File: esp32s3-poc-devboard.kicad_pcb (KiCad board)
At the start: 4 copper layers, 98 parts, among them J1 24VDC, J2 Conn_01x01_Pin, J3 USB_C_Receptacle_USB2.0_14P, J4 USB_C_Receptacle_USB2.0_14P, J5 Screw_Terminal_01x06, J6 Conn_Coaxial, J7 Conn_01x16_Pin, J8 Screw_Terminal_01x04, Q3 MMDT5551, SW1 SW_Push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

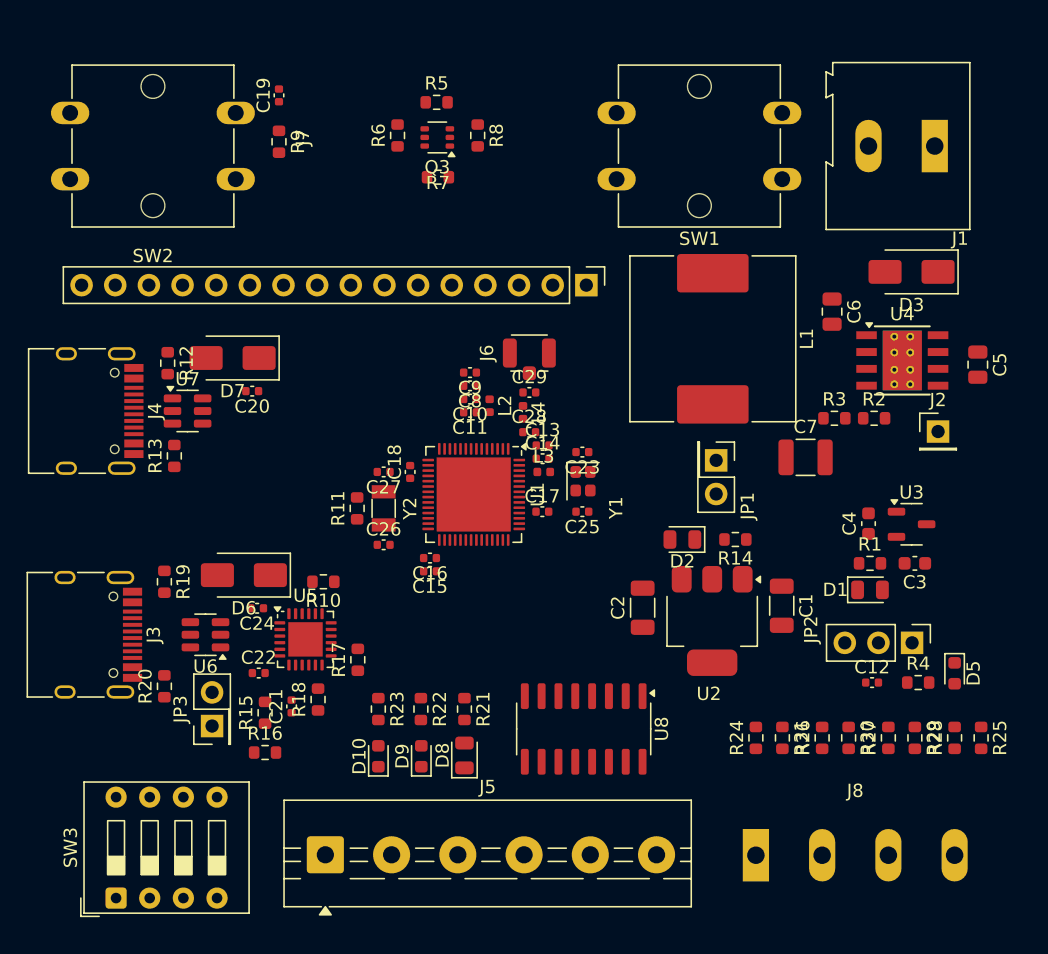
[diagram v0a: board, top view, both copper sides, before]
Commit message: clean up silkscreen
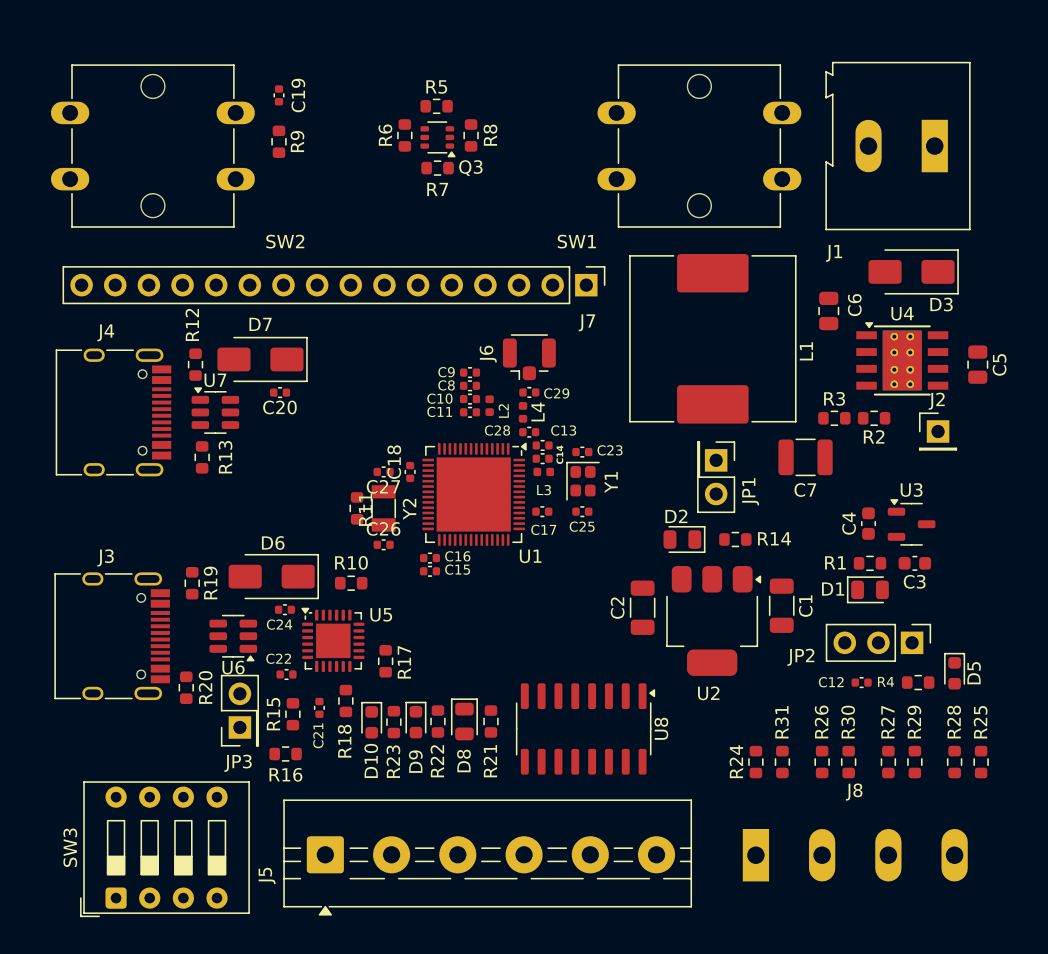
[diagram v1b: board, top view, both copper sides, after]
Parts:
- moved D10 2.61 mm to (147.5, 102.0), turned to -90 degrees
- moved D9 2.60 mm to (150.8, 102.0), turned to -90 degrees
- moved D8 2.56 mm to (154.5, 101.9), turned to -90 degrees
- moved R21 2.21 mm to (156.5, 101.9)
- moved C20 2.10 mm to (140.6, 77.1)
- moved C21 2.10 mm to (143.6, 100.9)
- moved JP3 2.10 mm to (137.6, 102.4)
- moved R15 2.10 mm to (141.6, 101.4)
- moved R17 2.10 mm to (148.6, 97.4)
- moved R18 2.10 mm to (145.6, 100.4)
- moved U6 2.10 mm to (137.1, 95.5)
- moved C22 2.10 mm to (141.1, 98.4)
- moved C24 2.10 mm to (140.9, 93.5)
- moved D6 2.10 mm to (139.9, 91.0)
- moved D7 2.10 mm to (139.1, 74.6)
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
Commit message: add board outline
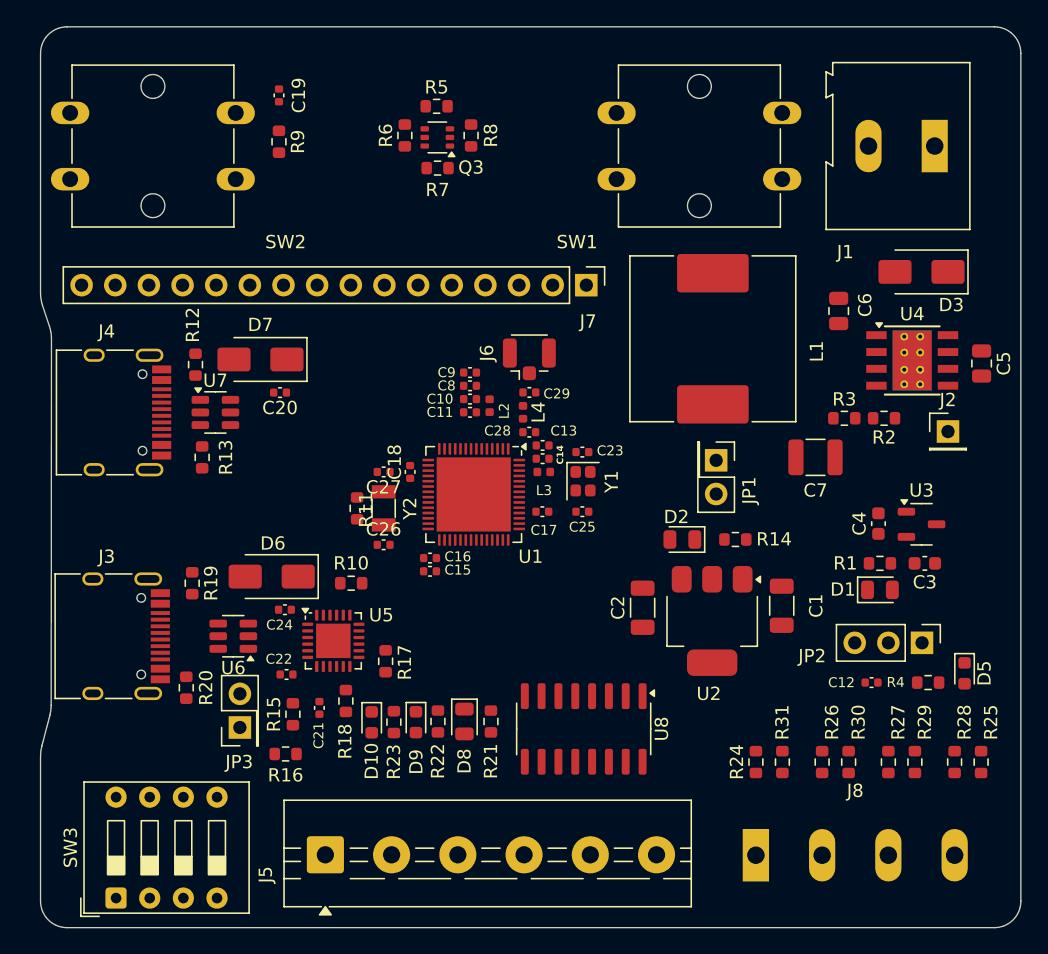
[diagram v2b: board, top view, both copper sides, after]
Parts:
- moved C12 0.75 mm to (185.2, 99.0)
- moved C3 0.75 mm to (189.2, 90.0)
- moved C4 0.75 mm to (185.8, 87.0)
- moved C6 0.75 mm to (182.8, 71.0)
- moved C7 0.75 mm to (181.0, 82.0)
- moved D1 0.75 mm to (185.9, 92.0)
- moved D3 0.75 mm to (189.0, 68.0)
- moved D5 0.75 mm to (192.2, 98.3)
- moved J2 0.75 mm to (191.0, 80.0)
- moved JP2 0.75 mm to (189.0, 96.0)
- moved R1 0.75 mm to (185.9, 90.0)
- moved R2 0.75 mm to (186.2, 79.0)
- moved R3 0.75 mm to (183.2, 79.0)
- moved R4 0.75 mm to (189.5, 99.0)
- moved U3 0.75 mm to (189.0, 87.0)
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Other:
- board outline added: 74 x 68 mm

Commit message: add inner ground layers
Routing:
- added copper zone on In1.Cu, net GND
- added copper zone on In2.Cu, net GND
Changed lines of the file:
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@@
 		(6 "In2.Cu" signal)
 		(2 "B.Cu" signal)
-		(9 "F.Adhes" user "F.Adhesive")
 		(11 "B.Adhes" user "B.Adhesive")
 		(13 "F.Paste" user)
@@
 		(1 "F.Mask" user)
 		(3 "B.Mask" user)
-		(17 "Dwgs.User" user "User.Drawings")
-		(19 "Cmts.User" user "User.Comments")
-		(21 "Eco1.User" user "User.Eco1")
-		(23 "Eco2.User" user "User.Eco2")
 		(25 "Edge.Cuts" user)
 		(27 "Margin" user)
@@
 		(layer "Edge.Cuts")
 	)
+	(zone
+		(net 1)
+		(net_name "GND")
+		(layers "In1.Cu" "In2.Cu")
+		(hatch edge 0.5)
+		(connect_pads
+			(clearance 0.3)
+		)
+		(min_thickness 0.15)
+		(filled_areas_thickness no)
+		(fill yes
+			(thermal_gap 0.4)
+			(thermal_bridge_width 0.25)
+		)
+		(polygon
+			(pts
+				(xy 196.5 49.5) (xy 196.5 117.5) (xy 122.5 117.5) (xy 122.5 49.5)
+			)
+		)
+	)
 	(embedded_fonts no)

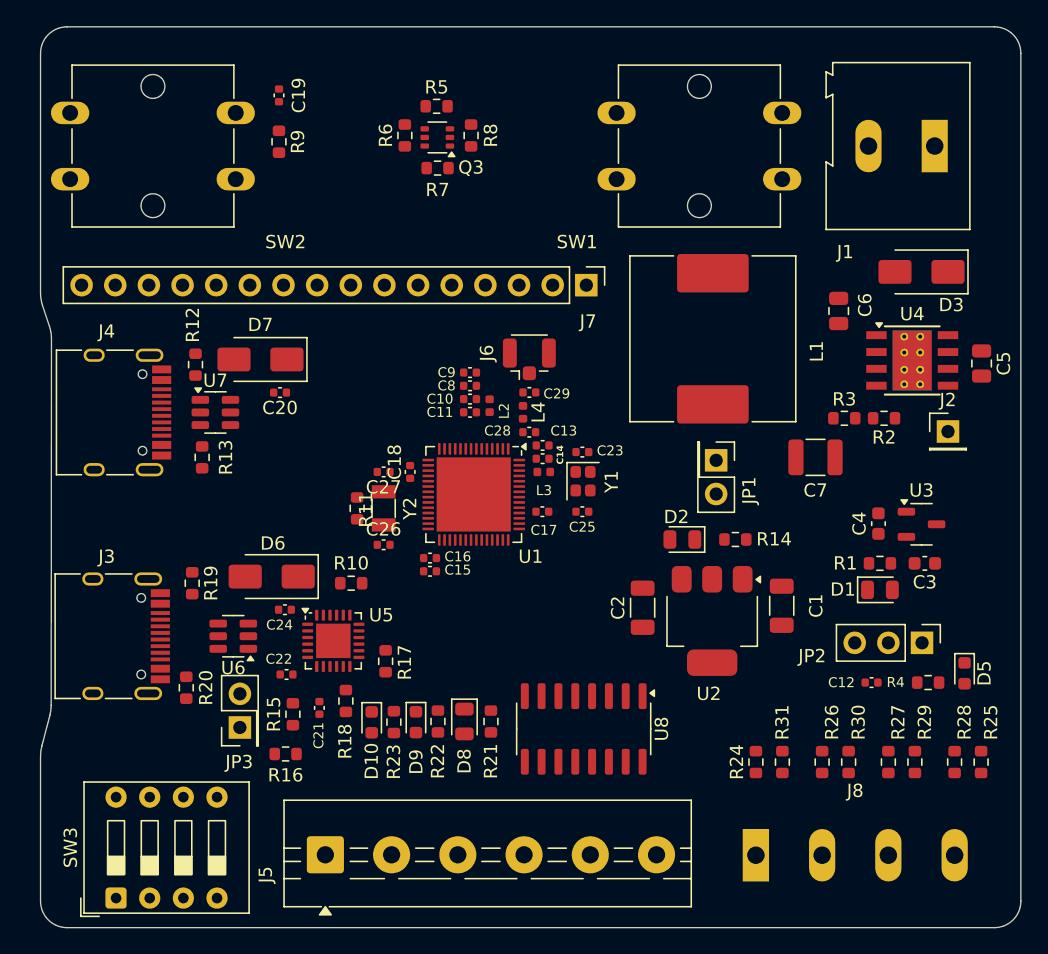
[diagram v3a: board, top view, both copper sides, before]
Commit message: add jlc tooling holes
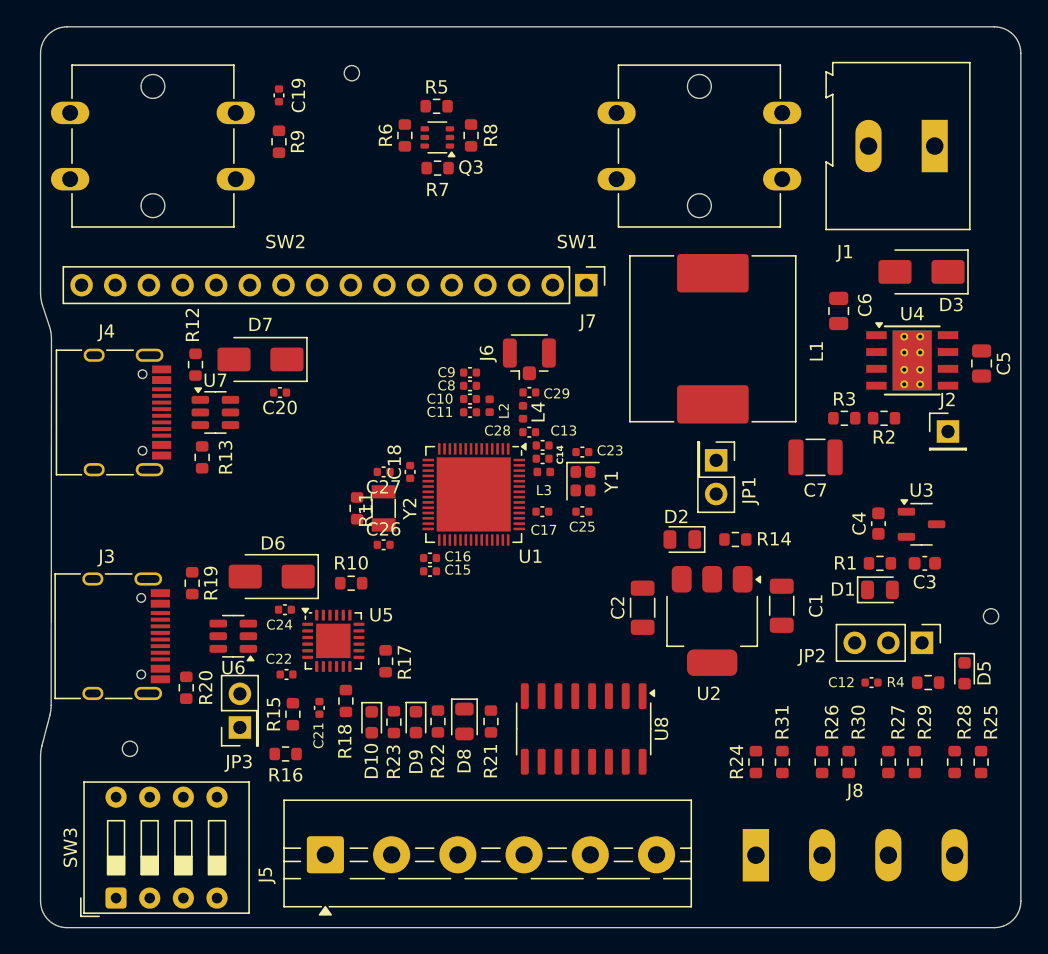
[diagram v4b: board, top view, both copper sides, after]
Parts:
- added ?: , , F.Cu at (194.2, 94.0)
- added ?: , , F.Cu at (146.0, 53.0)
- added REF**: ToolingHole_1.152mm, MountingHole:ToolingHole_1.152mm, F.Cu at (129.2, 104.0)
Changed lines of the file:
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@@
 		)
 	)
+	(footprint ""
+		(layer "F.Cu")
+		(at 194.25 94)
+		(property "Reference" ""
+			(at 0 0 0)
+			(layer "F.SilkS")
+			(effects
+				(font
+					(size 1.27 1.27)
+					(thickness 0.15)
+				)
+			)
+		)
+		(property "Value" ""
+			(at 0 0 0)
+			(layer "F.Fab")
+			(effects
+				(font
+					(size 1.27 1.27)
+					(thickness 0.15)
+				)
+			)
+		)
+		(property "Datasheet" ""
+			(at 0 0 0)
+			(layer "F.Fab")
+			(hide yes)
+			(effects
+				(font
+					(size 1.27 1.27)
+					(thickness 0.15)
+				)
+			)
+		)
+		(property "Description" ""
+			(at 0 0 0)
+			(layer "F.Fab")
+			(hide yes)
+			(effects
+				(font
+					(size 1.27 1.27)
+					(thickness 0.15)
+				)
+			)
+		)
+		(pad "" np_thru_hole circle
+			(at 0 0)
+			(size 1.152 1.152)
+			(drill 1.152)
+			(layers "F&B.Cu" "*.Mask")
+			(solder_mask_margin 0.074)
+		)
+		(embedded_fonts no)
+	)
 	(footprint "Resistor_SMD:R_0603_1608Metric"
 		(layer "F.Cu")
@@
 		)
 	)
+	(footprint ""
+		(layer "F.Cu")
+		(at 146 53)
+		(property "Reference" ""
+			(at 0 0 0)
+			(layer "F.SilkS")
+			(effects
+				(font
+					(size 1.27 1.27)
+					(thickness 0.15)
+				)
+			)
+		)
+		(property "Value" ""
+			(at 0 0 0)
+			(layer "F.Fab")
+			(effects
+				(font
+					(size 1.27 1.27)
+					(thickness 0.15)
+				)
+			)
+		)
+		(property "Datasheet" ""
+			(at 0 0 0)
+			(layer "F.Fab")
+			(hide yes)
+			(effects
+				(font
+					(size 1.27 1.27)
+					(thickness 0.15)
+				)
+			)
+		)
+		(property "Description" ""
+			(at 0 0 0)
+			(layer "F.Fab")
+			(hide yes)
+			(effects
+				(font
+					(size 1.27 1.27)
+					(thickness 0.15)
+				)
+			)
+		)
+		(pad "" np_thru_hole circle
+			(at 0 0)
+			(size 1.152 1.152)
+			(drill 1.152)
+			(layers "F&B.Cu" "*.Mask")
+			(solder_mask_margin 0.074)
+		)
+		(embedded_fonts no)
+	)
 	(footprint "Resistor_SMD:R_0603_1608Metric"
 		(layer "F.Cu")
@@
 		)
 	)
+	(footprint "MountingHole:ToolingHole_1.152mm"
+		(layer "F.Cu")
+		(at 129.25 104)
+		(descr "Tooling Hole 1.152mm, 1.3mm solder mask, JLCPCB specification, https://jlcpcb.com/help/article/How-to-add-tooling-holes-for-PCB-assembly-order")
+		(tags "mounting")
+		(property "Reference" "REF**"
+			(at 0 -1.5 0)
+			(layer "F.SilkS")
+			(hide yes)
+			(effects
+				(font
+					(size 1 1)
+					(thickness 0.15)
+				)
+			)
+		)
+		(property "Value" "ToolingHole_1.152mm"
+			(at 0 1.6 0)
+			(layer "F.Fab")
+			(effects
+				(font
+					(size 1 1)
+					(thickness 0.15)
+				)
+			)
+		)
+		(property "Datasheet" ""
+			(at 0 0 0)
+			(unlocked yes)
+			(layer "F.Fab")
+			(hide yes)
+			(effects
+				(font
+					(size 1.27 1.27)
+					(thickness 0.15)
+				)
+			)
+		)
+		(property "Description" ""
+			(at 0 0 0)
+			(unlocked yes)
+			(layer "F.Fab")
+			(hide yes)
+			(effects
+				(font
+					(size 1.27 1.27)
+					(thickness 0.15)
+				)
+			)
+		)
+		(attr exclude_from_pos_files exclude_from_bom)
+		(fp_circle
+			(center 0 0)
+			(end 0.7 0)
+			(stroke
+				(width 0.05)
+				(type solid)
+			)
+			(fill no)
+			(layer "F.CrtYd")
+		)
+		(fp_text user "${REFERENCE}"
+			(at 0 0 0)
+			(layer "F.Fab")
+			(effects
+				(font
+					(size 1 1)
+					(thickness 0.15)
+				)
+			)
+		)
+		(pad "" np_thru_hole circle
+			(at 0 0)
+			(size 1.152 1.152)
+			(drill 1.152)
+			(layers "F&B.Cu" "*.Mask")
+			(solder_mask_margin 0.074)
+		)
+		(zone
+			(net 0)
+			(net_name "")
+			(layers "F.Cu" "B.Cu" "In1.Cu" "In2.Cu")
+			(hatch edge 0.5)
+			(connect_pads
+				(clearance 0)
+			)
+			(min_thickness 0.25)
+			(filled_areas_thickness no)
+			(keepout
+				(tracks not_allowed)
+				(vias allowed)
+				(pads allowed)
+				(copperpour not_allowed)
+				(footprints not_allowed)
+			)
+			(placement
+				(enabled no)
+				(sheetname "")
+			)
+			(fill
+				(thermal_gap 0.5)
+				(thermal_bridge_width 0.5)
+			)
+			(polygon
+				(pts
+					(xy 129.95 104) (xy 129.929659 103.832479) (xy 129.869819 103.674694) (xy 129.773958 103.535814)
+					(xy 129.647645 103.423911) (xy 129.498223 103.345489) (xy 129.334376 103.305104) (xy 129.165624 103.305104)
+					(xy 129.001777 103.345489) (xy 128.852355 103.423911) (xy 128.726042 103.535814) (xy 128.630181 103.674694)
+					(xy 128.570341 103.832479) (xy 128.55 104) (xy 128.570341 104.167521) (xy 128.630181 104.325306)
+					(xy 128.726042 104.464186) (xy 128.852355 104.576089) (xy 129.001777 104.654511) (xy 129.165624 104.694896)
+					(xy 129.334376 104.694896) (xy 129.498223 104.654511) (xy 129.647645 104.576089) (xy 129.773958 104.464186)
+					(xy 129.869819 104.325306) (xy 129.929659 104.167521)
+				)
+			)
+		)
+		(embedded_fonts no)
+	)
 	(footprint "Resistor_SMD:R_0603_1608Metric"

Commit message: add M1 mounting holes
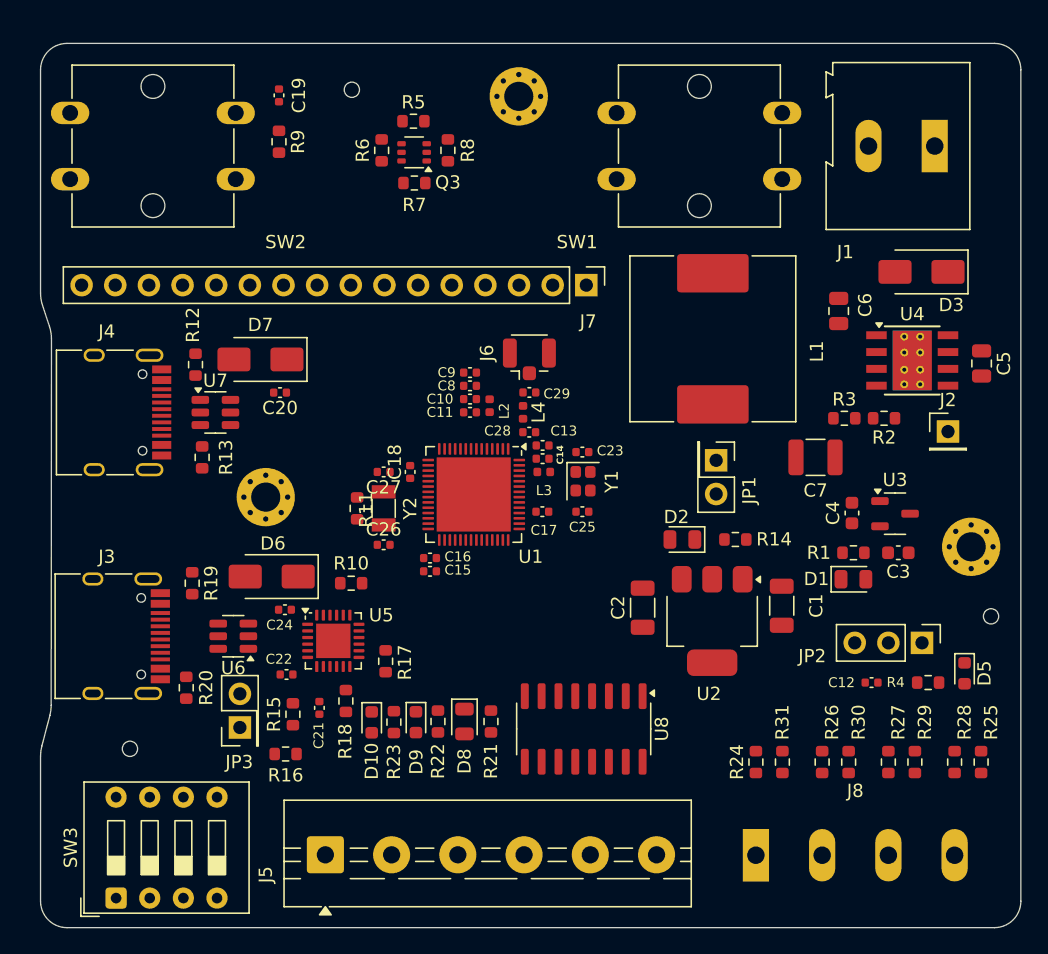
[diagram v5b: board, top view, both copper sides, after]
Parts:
- added REF**: MountingHole_2.2mm_M2_Pad_Via, MountingHole:MountingHole_2.2mm_M2_Pad_Via, F.Cu at (139.5, 85.0)
- added REF**: MountingHole_2.2mm_M2_Pad_Via, MountingHole:MountingHole_2.2mm_M2_Pad_Via, F.Cu at (158.6, 54.8)
- added REF**: MountingHole_2.2mm_M2_Pad_Via, MountingHole:MountingHole_2.2mm_M2_Pad_Via, F.Cu at (192.8, 88.8)
- moved C3 2.15 mm to (187.2, 89.2)
- moved C4 2.15 mm to (183.8, 86.2)
- moved D1 2.15 mm to (183.9, 91.2)
- moved R1 2.15 mm to (183.9, 89.2)
- moved U3 2.15 mm to (187.0, 86.2)
- moved Q3 2.08 mm to (150.7, 59.0)
- moved R5 2.08 mm to (150.7, 56.6)
- moved R6 2.08 mm to (148.2, 58.8)
- moved R7 2.08 mm to (150.7, 61.3)
- moved R8 2.08 mm to (153.2, 58.8)
- moved ? 1.25 mm to (146.0, 54.2)
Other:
- board size 74 x 68 mm -> 74 x 66.8 mm
